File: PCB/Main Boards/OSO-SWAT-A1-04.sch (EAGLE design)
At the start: 34 parts, among them J1 FH19C-9S-0.5SH_10_, U1 ATSAML22J18A-MUT, U2 MIC5365-3.3YC5-TR

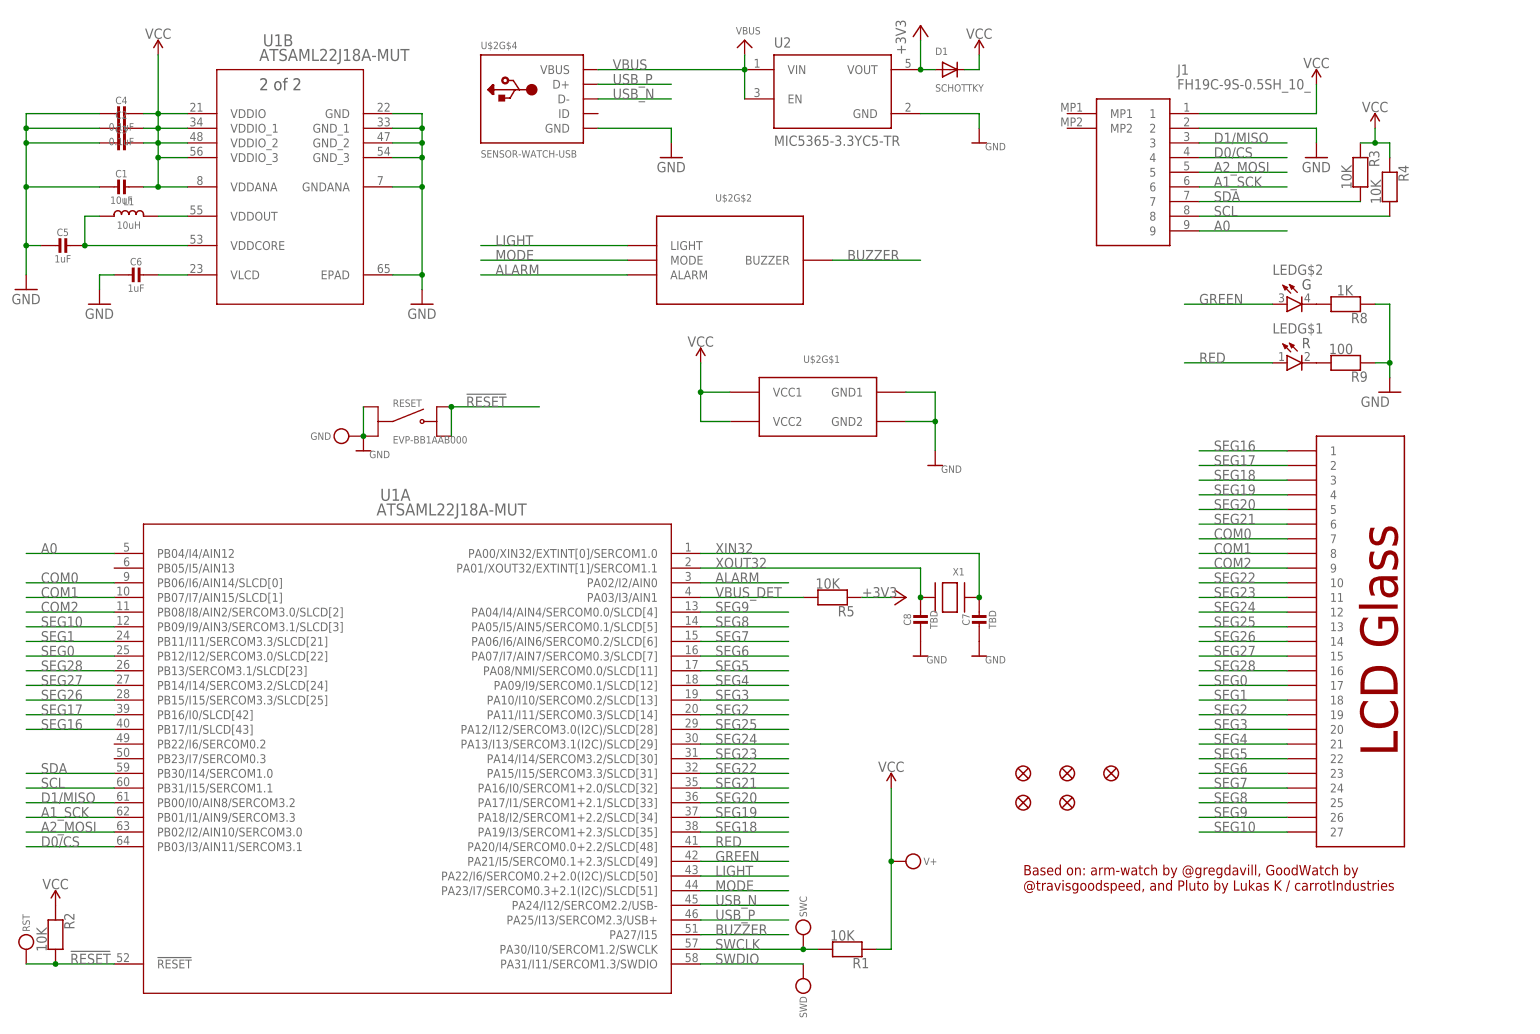
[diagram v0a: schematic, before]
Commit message: rename segments in schematic to match SLCD driver
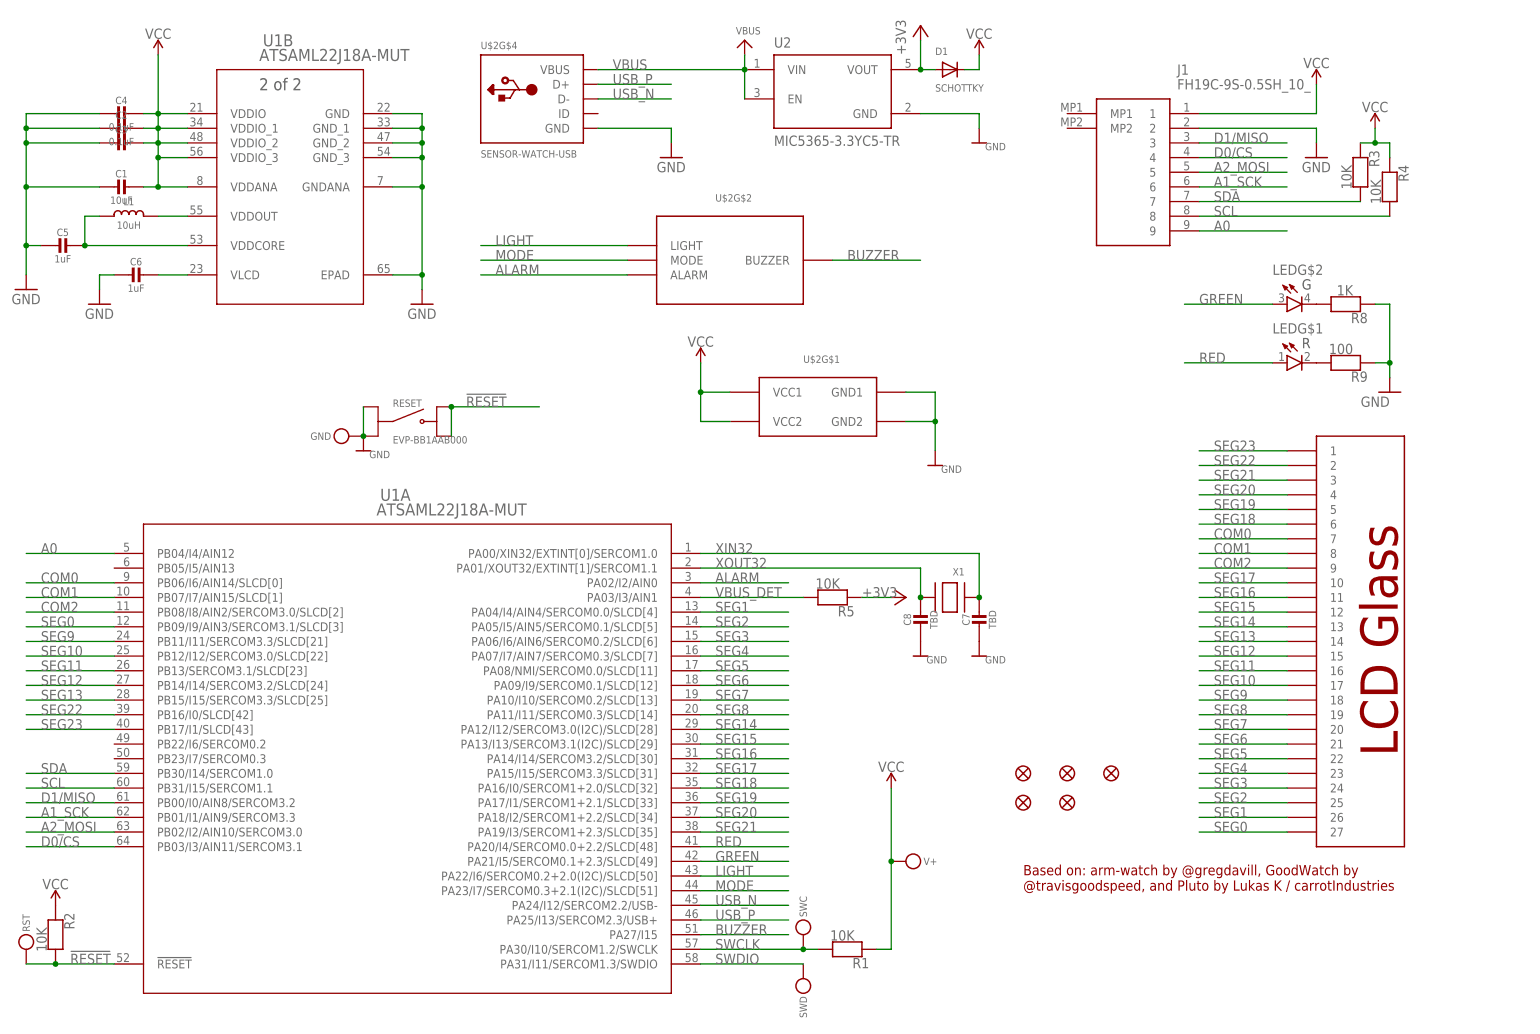
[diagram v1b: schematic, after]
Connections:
- net SEG24 renamed SEG15
- net SEG25 renamed SEG14
- net SEG26 renamed SEG13
- net SEG27 renamed SEG12
- net SEG28 renamed SEG11
- net SEG0: now also U$2G$3.27, U1A.PB09/I9/AIN3/SERCOM3.1/SLCD[3]; no longer U$2G$3.17, U1A.PB12/I12/SERCOM3.0/SLCD[22]
- net SEG1: now also U$2G$3.26, U1A.PA04/I4/AIN4/SERCOM0.0/SLCD[4]; no longer U$2G$3.18, U1A.PB11/I11/SERCOM3.3/SLCD[21]
- net SEG10: now also U$2G$3.17, U1A.PB12/I12/SERCOM3.0/SLCD[22]; no longer U$2G$3.27, U1A.PB09/I9/AIN3/SERCOM3.1/SLCD[3]
- net SEG16: now also U$2G$3.11, U1A.PA14/I14/SERCOM3.2/SLCD[30]; no longer U$2G$3.1, U1A.PB17/I1/SLCD[43]
- net SEG17: now also U$2G$3.10, U1A.PA15/I15/SERCOM3.3/SLCD[31]; no longer U$2G$3.2, U1A.PB16/I0/SLCD[42]
- net SEG18: now also U$2G$3.6, U1A.PA16/I0/SERCOM1+2.0/SLCD[32]; no longer U$2G$3.3, U1A.PA19/I3/SERCOM1+2.3/SLCD[35]
- net SEG19: now also U$2G$3.5, U1A.PA17/I1/SERCOM1+2.1/SLCD[33]; no longer U$2G$3.4, U1A.PA18/I2/SERCOM1+2.2/SLCD[34]
- net SEG2: now also U$2G$3.25, U1A.PA05/I5/AIN5/SERCOM0.1/SLCD[5]; no longer U$2G$3.19, U1A.PA11/I11/SERCOM0.3/SLCD[14]
- net SEG20: now also U$2G$3.4, U1A.PA18/I2/SERCOM1+2.2/SLCD[34]; no longer U$2G$3.5, U1A.PA17/I1/SERCOM1+2.1/SLCD[33]
- net SEG21: now also U$2G$3.3, U1A.PA19/I3/SERCOM1+2.3/SLCD[35]; no longer U$2G$3.6, U1A.PA16/I0/SERCOM1+2.0/SLCD[32]
- net SEG22: now also U$2G$3.2, U1A.PB16/I0/SLCD[42]; no longer U$2G$3.10, U1A.PA15/I15/SERCOM3.3/SLCD[31]
- net SEG23: now also U$2G$3.1, U1A.PB17/I1/SLCD[43]; no longer U$2G$3.11, U1A.PA14/I14/SERCOM3.2/SLCD[30]
- net SEG3: now also U$2G$3.24, U1A.PA06/I6/AIN6/SERCOM0.2/SLCD[6]; no longer U$2G$3.20, U1A.PA10/I10/SERCOM0.2/SLCD[13]
- net SEG4: now also U$2G$3.23, U1A.PA07/I7/AIN7/SERCOM0.3/SLCD[7]; no longer U$2G$3.21, U1A.PA09/I9/SERCOM0.1/SLCD[12]
- net SEG6: now also U$2G$3.21, U1A.PA09/I9/SERCOM0.1/SLCD[12]; no longer U$2G$3.23, U1A.PA07/I7/AIN7/SERCOM0.3/SLCD[7]
- net SEG7: now also U$2G$3.20, U1A.PA10/I10/SERCOM0.2/SLCD[13]; no longer U$2G$3.24, U1A.PA06/I6/AIN6/SERCOM0.2/SLCD[6]
- net SEG8: now also U$2G$3.19, U1A.PA11/I11/SERCOM0.3/SLCD[14]; no longer U$2G$3.25, U1A.PA05/I5/AIN5/SERCOM0.1/SLCD[5]
- net SEG9: now also U$2G$3.18, U1A.PB11/I11/SERCOM3.3/SLCD[21]; no longer U$2G$3.26, U1A.PA04/I4/AIN4/SERCOM0.0/SLCD[4]
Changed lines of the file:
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@@
 </segment>
 </net>
-<net name="SEG16" class="0">
+<net name="SEG23" class="0">
 <segment>
 <wire x1="215.9" y1="101.6" x2="231.14" y2="101.6" width="0.1524" layer="91"/>
@@
 </segment>
 </net>
-<net name="SEG17" class="0">
+<net name="SEG22" class="0">
 <segment>
 <wire x1="215.9" y1="99.06" x2="231.14" y2="99.06" width="0.1524" layer="91"/>
@@
 </segment>
 </net>
-<net name="SEG18" class="0">
+<net name="SEG21" class="0">
 <segment>
 <wire x1="215.9" y1="96.52" x2="231.14" y2="96.52" width="0.1524" layer="91"/>
@@
 </segment>
 </net>
-<net name="SEG19" class="0">
+<net name="SEG20" class="0">
 <segment>
 <wire x1="215.9" y1="93.98" x2="231.14" y2="93.98" width="0.1524" layer="91"/>
@@
 </segment>
 </net>
-<net name="SEG20" class="0">
+<net name="SEG19" class="0">
 <segment>
 <wire x1="215.9" y1="91.44" x2="231.14" y2="91.44" width="0.1524" layer="91"/>
@@
 </segment>
 </net>
-<net name="SEG21" class="0">
+<net name="SEG18" class="0">
 <segment>
 <wire x1="215.9" y1="88.9" x2="231.14" y2="88.9" width="0.1524" layer="91"/>
@@
 </segment>
 </net>
-<net name="SEG22" class="0">
+<net name="SEG17" class="0">
 <segment>
 <wire x1="215.9" y1="78.74" x2="231.14" y2="78.74" width="0.1524" layer="91"/>
@@
 </segment>
 </net>
-<net name="SEG23" class="0">
+<net name="SEG16" class="0">
 <segment>
 <wire x1="215.9" y1="76.2" x2="231.14" y2="76.2" width="0.1524" layer="91"/>
@@
 </segment>
 </net>
-<net name="SEG24" class="0">
+<net name="SEG15" class="0">
 <segment>
 <wire x1="215.9" y1="73.66" x2="231.14" y2="73.66" width="0.1524" layer="91"/>
@@
 </segment>
 </net>
-<net name="SEG25" class="0">
+<net name="SEG14" class="0">
 <segment>
 <wire x1="215.9" y1="71.12" x2="231.14" y2="71.12" width="0.1524" layer="91"/>
@@
 </segment>
 </net>
-<net name="SEG26" class="0">
+<net name="SEG13" class="0">
 <segment>
 <wire x1="215.9" y1="68.58" x2="231.14" y2="68.58" width="0.1524" layer="91"/>
@@
 </segment>
 </net>
-<net name="SEG27" class="0">
+<net name="SEG12" class="0">
 <segment>
 <wire x1="215.9" y1="66.04" x2="231.14" y2="66.04" width="0.1524" layer="91"/>
@@
 </segment>
 </net>
-<net name="SEG28" class="0">
+<net name="SEG11" class="0">
 <segment>
 <wire x1="215.9" y1="63.5" x2="231.14" y2="63.5" width="0.1524" layer="91"/>
@@
 </segment>
 </net>
-<net name="SEG0" class="0">
+<net name="SEG10" class="0">
 <segment>
 <wire x1="215.9" y1="60.96" x2="231.14" y2="60.96" width="0.1524" layer="91"/>
@@
 </segment>
 </net>
-<net name="SEG1" class="0">
+<net name="SEG9" class="0">
 <segment>
 <wire x1="215.9" y1="58.42" x2="231.14" y2="58.42" width="0.1524" layer="91"/>
@@
 </segment>
 </net>
-<net name="SEG2" class="0">
+<net name="SEG8" class="0">
 <segment>
 <wire x1="215.9" y1="55.88" x2="231.14" y2="55.88" width="0.1524" layer="91"/>
@@
 </segment>
 </net>
-<net name="SEG3" class="0">
+<net name="SEG7" class="0">
 <segment>
 <wire x1="215.9" y1="53.34" x2="231.14" y2="53.34" width="0.1524" layer="91"/>
@@
 </segment>
 </net>
-<net name="SEG4" class="0">
+<net name="SEG6" class="0">
 <segment>
 <wire x1="215.9" y1="50.8" x2="231.14" y2="50.8" width="0.1524" layer="91"/>
@@
 </segment>
 </net>
-<net name="SEG6" class="0">
+<net name="SEG4" class="0">
 <segment>
 <wire x1="215.9" y1="45.72" x2="231.14" y2="45.72" width="0.1524" layer="91"/>
@@
 </segment>
 </net>
-<net name="SEG7" class="0">
+<net name="SEG3" class="0">
 <segment>
 <wire x1="215.9" y1="43.18" x2="231.14" y2="43.18" width="0.1524" layer="91"/>
@@
 </segment>
 </net>
-<net name="SEG8" class="0">
+<net name="SEG2" class="0">
 <segment>
 <wire x1="215.9" y1="40.64" x2="231.14" y2="40.64" width="0.1524" layer="91"/>
@@
 </segment>
 </net>
-<net name="SEG9" class="0">
+<net name="SEG1" class="0">
 <segment>
 <wire x1="215.9" y1="38.1" x2="231.14" y2="38.1" width="0.1524" layer="91"/>
@@
 </segment>
 </net>
-<net name="SEG10" class="0">
+<net name="SEG0" class="0">
 <segment>
 <wire x1="215.9" y1="35.56" x2="231.14" y2="35.56" width="0.1524" layer="91"/>

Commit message: fix LED part number, make boards identical
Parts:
- LED: value QBLP655R -> QBLP655-RIG; device QBLP655R:QBLP655R -> QBLP655:QBLP655-RIG
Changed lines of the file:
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@@
 <part name="+3V1" library="supply1" library_urn="urn:adsk.eagle:library:371" deviceset="+3V3" device=""/>
 <part name="RESET" library="EVP-BB1AAB000" deviceset="EVP-BB1AAB000" device=""/>
-<part name="LED" library="QBLP655R" deviceset="QBLP655R" device=""/>
 <part name="GND15" library="supply1" deviceset="GND" device=""/>
 <part name="R8" library="microbuilder" deviceset="RESISTOR" device="_0603MP" value="1K"/>
@@
 <attribute name="REV" value="A"/>
 </part>
+<part name="LED" library="QBLP655" deviceset="QBLP655-RIG" device=""/>
 </parts>
 <sheets>
@@
 <attribute name="VALUE" x="76.2" y="104.14" size="1.27" layer="96" align="top-left"/>
 </instance>
-<instance part="LED" gate="G$1" x="231.14" y="116.84" smashed="yes">
-<attribute name="NAME" x="228.6" y="121.92" size="1.780740625" layer="95"/>
-</instance>
-<instance part="LED" gate="G$2" x="231.14" y="127" smashed="yes">
-<attribute name="NAME" x="228.6" y="132.08" size="1.780740625" layer="95"/>
-</instance>
 <instance part="GND15" gate="1" x="248.92" y="111.76" smashed="yes" rot="MR0">
 <attribute name="VALUE" x="248.92" y="109.22" size="1.778" layer="96" rot="MR0"/>
@@
 <instance part="FID4" gate="G$1" x="193.04" y="40.64" smashed="yes"/>
 <instance part="FID6" gate="G$1" x="185.42" y="40.64" smashed="yes"/>
+<instance part="LED" gate="G$1" x="231.14" y="116.84" smashed="yes"/>
+<instance part="LED" gate="G$2" x="231.14" y="127" smashed="yes"/>
 </instances>
 <busses>
